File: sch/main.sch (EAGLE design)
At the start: 6 parts, among them U1 LF33ABDT-TR

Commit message: [ update ] schematics, rotary switch util
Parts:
- added C5, C7: 47u, rcl:CPOL-EUD
- added C6, C8: 100n, rcl:C-EUC1206K
- added CON_LED, CON_POWER: (no value), pinhead:PINHD-1X3
- added CON_START: (no value), pinhead:PINHD-1X2
- added R1, R12: 2M, resistor:R-US_R1206
- added R10, R22: 2.22K, resistor:R-US_R1206
- added R11, R23: 1K, resistor:R-US_R1206
- added R13, R24: 10K, resistor:R-US_R1206
- added R14, R2: 100K, resistor:R-US_R1206
- added R15, R3: 45K, resistor:R-US_R1206
- added R16, R4: 27K, resistor:R-US_R1206
- added R17, R5: 17.5K, resistor:R-US_R1206
- added R18, R6: 12K, resistor:R-US_R1206
- added R19, R7: 8.33K, resistor:R-US_R1206
- added R20, R8: 5.715K, resistor:R-US_R1206
- added R21, R9: 3.75K, resistor:R-US_R1206
- added SW_MODE, SW_POS: 50-1POLE30, switch:50-1POLE30
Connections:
- new net BUT_START: CON_START.1, U$1.A0
- new net LED_FAIL: CON_LED.2, U$1.A4
- new net LED_WIP: CON_LED.1, U$1.A3
- new net N$10: R9.2, SW_MODE.9
- new net N$11: R10.2, SW_MODE.10
- new net N$12: R11.2, SW_MODE.11
- new net N$13: R12.2, SW_POS.1
- new net N$14: R14.2, SW_POS.2
- new net N$15: R15.2, SW_POS.3
- new net N$16: R16.2, SW_POS.4
- new net N$17: R17.2, SW_POS.5
- new net N$18: R18.2, SW_POS.6
- new net N$19: R19.2, SW_POS.7
- new net N$2: R2.2, SW_MODE.2
- new net N$20: R20.2, SW_POS.8
- new net N$21: R21.2, SW_POS.9
- new net N$22: R22.2, SW_POS.10
- new net N$23: R23.2, SW_POS.11
- new net N$4: U$1.ANT
- new net N$5: R4.2, SW_MODE.4
- new net N$6: R5.2, SW_MODE.5
- new net N$7: R6.2, SW_MODE.6
- new net N$8: R7.2, SW_MODE.7
- new net N$9: R8.2, SW_MODE.8
- new net SW_MODE: R1.1, R10.1, R11.1, R13.2, R2.1, R3.1, R4.1, R5.1, R6.1, R7.1, R8.1, R9.1, SW_MODE.12, U$1.A1
- new net SW_POS: R12.1, R14.1, R15.1, R16.1, R17.1, R18.1, R19.1, R20.1, R21.1, R22.1, R23.1, R24.2, SW_POS.12, U$1.A2
- new net VBAT_45: CON_POWER.1
- new net VBAT_ON: C2.1, C3.+, C5.+, C6.1, CON_POWER.2, U$1.VIN, U1.INPUT
- new net VREG_33: C1.1, C4.+, C7.+, C8.1, SW_MODE.A, SW_POS.A, U$1.3.3@1, U$1.3.3@2, U$1.AREF, U1.OUT
- net GND: now also C5.-, C6.2, C7.-, C8.2, CON_LED.3, CON_POWER.3, CON_START.2, R13.1, R24.1, U$1.GND@1, U$1.GND@2
- net N$1: now also R1.2, SW_MODE.1; no longer C2.1, C3.+, U1.INPUT
- net N$3: now also R3.2, SW_MODE.3; no longer C1.1, C4.+, U1.OUT
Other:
- note added: "TOREMOVE, onboard LDO used"
- moved on the sheet: C1, C2, C3, C4, U1

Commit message: [ update ] schematics, bom
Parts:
- removed C1, C2: 100n, rcl:C-EUC1206K
- removed C3, C4: 47u, rcl:CPOL-EUD
- removed U1: LF33ABDT-TR, STM-LF33ABDT-TR@E:LF33ABDT-TR
- added R25, R26: 330, resistor:R-US_R1206
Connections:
- new net N$24: CON_LED.1, R25.2
- new net N$25: CON_LED.2, R26.2
- net GND: no longer C1.2, C2.2, C3.-, C4.-, U1.GND
- net LED_FAIL: now also R26.1; no longer CON_LED.2
- net LED_WIP: now also R25.1; no longer CON_LED.1
- net VBAT_ON: no longer C2.1, C3.+, U1.INPUT
- net VREG_33: no longer C1.1, C4.+, U1.OUT
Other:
- note added: "connect to led+"
- note removed: "TOREMOVE, onboard LDO used"
- note removed: "actually a BA033CC0FP"
- moved on the sheet: C5, C6, C7, C8, CON_LED, CON_POWER, CON_START, R1, R10, R11, R12, R13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

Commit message: [ add ] main.brd pinhdr_13.lbr
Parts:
- added CON_ANT: (no value), pinhead:PINHD-1X2
- added CON_MODE, CON_POS: PINHDR_13, pinhdr_13:PINHDR_13
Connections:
- removed net N$4: U$1.ANT
- new net ANT: CON_ANT.1, U$1.ANT
- net GND: now also CON_ANT.2
- net N$1: now also CON_MODE.1; no longer SW_MODE.1
- net N$10: now also CON_MODE.9; no longer SW_MODE.9
- net N$11: now also CON_MODE.10; no longer SW_MODE.10
- net N$12: now also CON_MODE.11; no longer SW_MODE.11
- net N$13: now also CON_POS.1; no longer SW_POS.1
- net N$14: now also CON_POS.2; no longer SW_POS.2
- net N$15: now also CON_POS.3; no longer SW_POS.3
- net N$16: now also CON_POS.4; no longer SW_POS.4
- net N$17: now also CON_POS.5; no longer SW_POS.5
- net N$18: now also CON_POS.6; no longer SW_POS.6
- net N$19: now also CON_POS.7; no longer SW_POS.7
- net N$2: now also CON_MODE.2; no longer SW_MODE.2
- net N$20: now also CON_POS.8; no longer SW_POS.8
- net N$21: now also CON_POS.9; no longer SW_POS.9
- net N$22: now also CON_POS.10; no longer SW_POS.10
- net N$23: now also CON_POS.11; no longer SW_POS.11
- net N$3: now also CON_MODE.3; no longer SW_MODE.3
- net N$5: now also CON_MODE.4; no longer SW_MODE.4
- net N$6: now also CON_MODE.5; no longer SW_MODE.5
- net N$7: now also CON_MODE.6; no longer SW_MODE.6
- net N$8: now also CON_MODE.7; no longer SW_MODE.7
- net N$9: now also CON_MODE.8; no longer SW_MODE.8
- net SW_MODE: now also CON_MODE.12; no longer SW_MODE.12
- net SW_POS: now also CON_POS.12; no longer SW_POS.12
- net VREG_33: now also CON_MODE.13, CON_POS.13; no longer SW_MODE.A, SW_POS.A
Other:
- moved on the sheet: SW_MODE, SW_POS

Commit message: [ update ] schematics, routing
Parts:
- CON_ANT: value (none) -> BU-SMA-G; device pinhead:PINHD-1X2 -> con-coax:BU-SMA-G
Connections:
- net ANT: now also CON_ANT.2; no longer CON_ANT.1
- net GND: now also CON_ANT.1; no longer CON_ANT.2
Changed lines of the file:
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@@
 <part name="SW_MODE" library="switch" deviceset="50-1POLE30" device=""/>
 <part name="CON_POS" library="pinhdr_13" deviceset="PINHDR_13" device=""/>
-<part name="CON_ANT" library="pinhead" deviceset="PINHD-1X2" device=""/>
+<part name="CON_ANT" library="con-coax" deviceset="BU-SMA-G" device=""/>
 </parts>
 <sheets>
@@
 <instance part="SW_MODE" gate="G$1" x="-2.54" y="-27.94" rot="R270"/>
 <instance part="CON_POS" gate="G$1" x="73.66" y="-27.94"/>
-<instance part="CON_ANT" gate="G$1" x="-45.72" y="48.26"/>
+<instance part="CON_ANT" gate="G1" x="-53.34" y="50.8"/>
 </instances>
 <busses>
@@
 </segment>
 <segment>
-<pinref part="CON_ANT" gate="G$1" pin="2"/>
-<wire x1="-48.26" y1="48.26" x2="-68.58" y2="48.26" width="0.1524" layer="91"/>
-<label x="-68.58" y="48.26" size="1.778" layer="95"/>
+<pinref part="CON_ANT" gate="G1" pin="1"/>
+<wire x1="-50.8" y1="50.8" x2="-43.18" y2="50.8" width="0.1524" layer="91"/>
+<label x="-48.26" y="50.8" size="1.778" layer="95"/>
 </segment>
 </net>
@@
 </segment>
 <segment>
-<pinref part="CON_ANT" gate="G$1" pin="1"/>
-<wire x1="-48.26" y1="50.8" x2="-68.58" y2="50.8" width="0.1524" layer="91"/>
-<label x="-68.58" y="50.8" size="1.778" layer="95"/>
+<pinref part="CON_ANT" gate="G1" pin="2"/>
+<wire x1="-50.8" y1="48.26" x2="-43.18" y2="48.26" width="0.1524" layer="91"/>
+<label x="-48.26" y="48.26" size="1.778" layer="95"/>
 </segment>
 </net>

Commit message: [ update ] schematics, routing
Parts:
- removed SW_MODE, SW_POS: 50-1POLE30, switch:50-1POLE30
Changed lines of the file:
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@@
 <part name="R25" library="resistor" deviceset="R-US_" device="R1206" value="330"/>
 <part name="R26" library="resistor" deviceset="R-US_" device="R1206" value="330"/>
-<part name="SW_POS" library="switch" deviceset="50-1POLE30" device=""/>
 <part name="CON_MODE" library="pinhdr_13" deviceset="PINHDR_13" device=""/>
-<part name="SW_MODE" library="switch" deviceset="50-1POLE30" device=""/>
 <part name="CON_POS" library="pinhdr_13" deviceset="PINHDR_13" device=""/>
 <part name="CON_ANT" library="con-coax" deviceset="BU-SMA-G" device=""/>
@@
 <instance part="R25" gate="G$1" x="-58.42" y="10.16"/>
 <instance part="R26" gate="G$1" x="-58.42" y="7.62"/>
-<instance part="SW_POS" gate="G$1" x="91.44" y="-27.94" rot="R270"/>
 <instance part="CON_MODE" gate="G$1" x="-20.32" y="-27.94"/>
-<instance part="SW_MODE" gate="G$1" x="-2.54" y="-27.94" rot="R270"/>
 <instance part="CON_POS" gate="G$1" x="73.66" y="-27.94"/>
 <instance part="CON_ANT" gate="G1" x="-53.34" y="50.8"/>

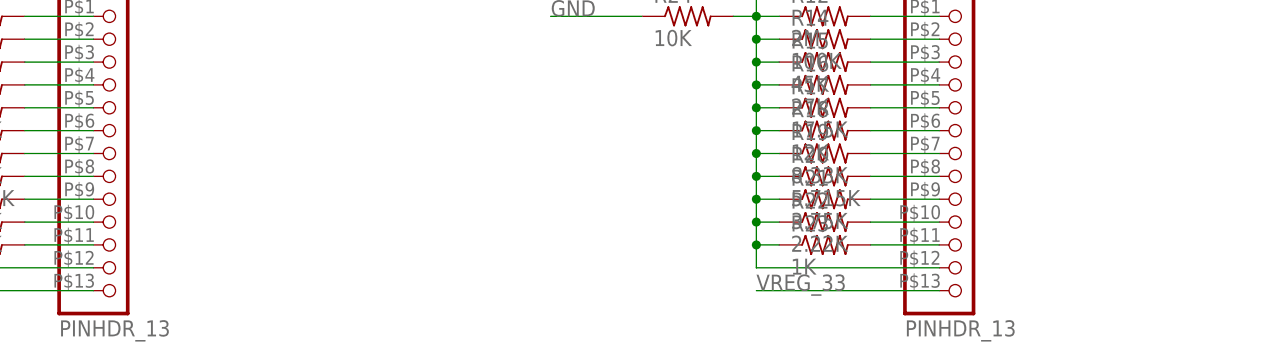
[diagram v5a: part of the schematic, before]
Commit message: [ update ] silkscreen cleaned
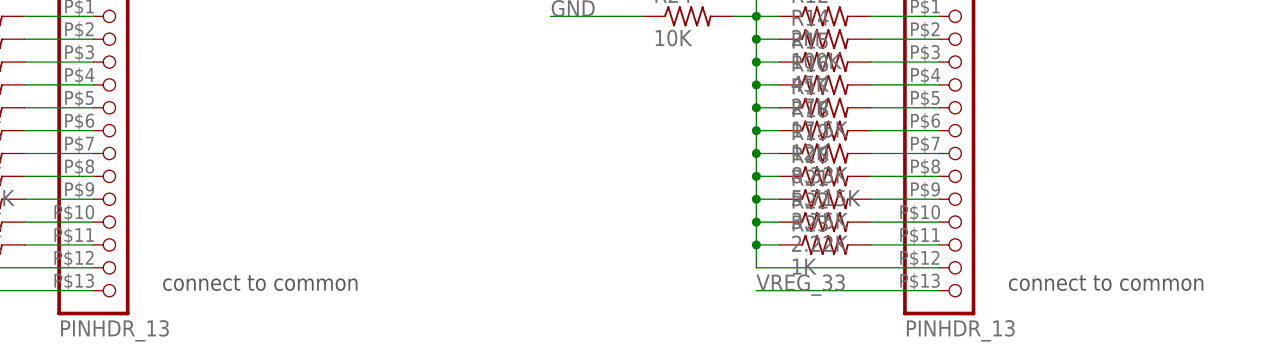
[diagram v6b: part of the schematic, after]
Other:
- note added: "connect to common"
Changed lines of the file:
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@@
 <text x="-43.18" y="10.16" size="1.778" layer="97">connect to led+</text>
 <text x="-43.18" y="7.62" size="1.778" layer="97">connect to led+</text>
+<text x="-15.24" y="-43.18" size="1.778" layer="97">connect to common</text>
+<text x="78.74" y="-43.18" size="1.778" layer="97">connect to common</text>
 </plain>
 <instances>

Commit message: [ update ] schematics frame
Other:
- note added: "https://github.com/texane/ooklone"
- note added: "ooklone_v000"
- note added: "texane@gmail.com"
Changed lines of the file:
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@@
 <part name="CON_POS" library="pinhdr_13" deviceset="PINHDR_13" device=""/>
 <part name="CON_ANT" library="con-coax" deviceset="BU-SMA-G" device=""/>
+<part name="FRAME1" library="frames" deviceset="A4L-LOC" device=""/>
 </parts>
 <sheets>
@@
 <text x="-15.24" y="-43.18" size="1.778" layer="97">connect to common</text>
 <text x="78.74" y="-43.18" size="1.778" layer="97">connect to common</text>
+<text x="53.34" y="-63.5" size="1.778" layer="94" font="vector">ooklone_v000</text>
+<text x="53.34" y="-68.58" size="1.778" layer="94" font="vector">https://github.com/texane/ooklone</text>
+<text x="53.34" y="-73.66" size="1.778" layer="94" font="vector">texane@gmail.com</text>
 </plain>
 <instances>
@@
 <instance part="CON_POS" gate="G$1" x="73.66" y="-27.94"/>
 <instance part="CON_ANT" gate="G1" x="-53.34" y="50.8"/>
+<instance part="FRAME1" gate="G$1" x="-111.76" y="-83.82" smashed="yes">
+<attribute name="DRAWING_NAME" x="105.41" y="-68.58" size="2.54" layer="94" font="vector"/>
+<attribute name="LAST_DATE_TIME" x="105.41" y="-73.66" size="2.286" layer="94" font="vector"/>
+<attribute name="SHEET" x="118.745" y="-78.74" size="2.54" layer="94" font="vector"/>
+</instance>
 </instances>
 <busses>

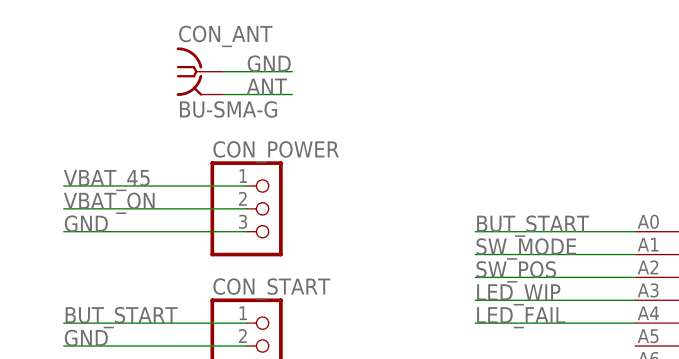
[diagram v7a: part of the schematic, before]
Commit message: [ fix ] gnd ant signal inversion
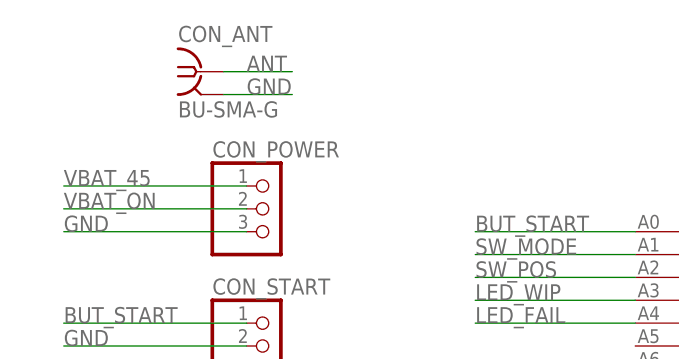
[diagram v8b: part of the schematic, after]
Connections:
- net ANT: now also CON_ANT.1; no longer CON_ANT.2
- net GND: now also CON_ANT.2; no longer CON_ANT.1
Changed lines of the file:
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@@
 <setting verticaltext="up"/>
 </settings>
-<grid distance="0.1" unitdist="inch" unit="inch" style="lines" multiple="1" display="yes" altdistance="0.01" altunitdist="inch" altunit="inch"/>
+<grid distance="0.1" unitdist="inch" unit="inch" style="lines" multiple="1" display="no" altdistance="0.01" altunitdist="inch" altunit="inch"/>
 <layers>
 <layer number="1" name="Top" color="4" fill="1" visible="no" active="no"/>
@@
 </segment>
 <segment>
-<pinref part="CON_ANT" gate="G1" pin="1"/>
-<wire x1="-50.8" y1="50.8" x2="-43.18" y2="50.8" width="0.1524" layer="91"/>
-<label x="-48.26" y="50.8" size="1.778" layer="95"/>
+<pinref part="CON_ANT" gate="G1" pin="2"/>
+<wire x1="-50.8" y1="48.26" x2="-43.18" y2="48.26" width="0.1524" layer="91"/>
+<label x="-48.26" y="48.26" size="1.778" layer="95"/>
 </segment>
 </net>
@@
 </segment>
 <segment>
-<pinref part="CON_ANT" gate="G1" pin="2"/>
-<wire x1="-50.8" y1="48.26" x2="-43.18" y2="48.26" width="0.1524" layer="91"/>
-<label x="-48.26" y="48.26" size="1.778" layer="95"/>
+<pinref part="CON_ANT" gate="G1" pin="1"/>
+<wire x1="-50.8" y1="50.8" x2="-43.18" y2="50.8" width="0.1524" layer="91"/>
+<label x="-48.26" y="50.8" size="1.778" layer="95"/>
 </segment>
 </net>
